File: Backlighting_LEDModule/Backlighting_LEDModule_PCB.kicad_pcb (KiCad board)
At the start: 2 copper layers, 32.2 x 55 mm, 6 parts, among them J1 Conn_02x10_Odd_Even, J11 BOARD_CONN, J2 Conn_02x10_Odd_Even

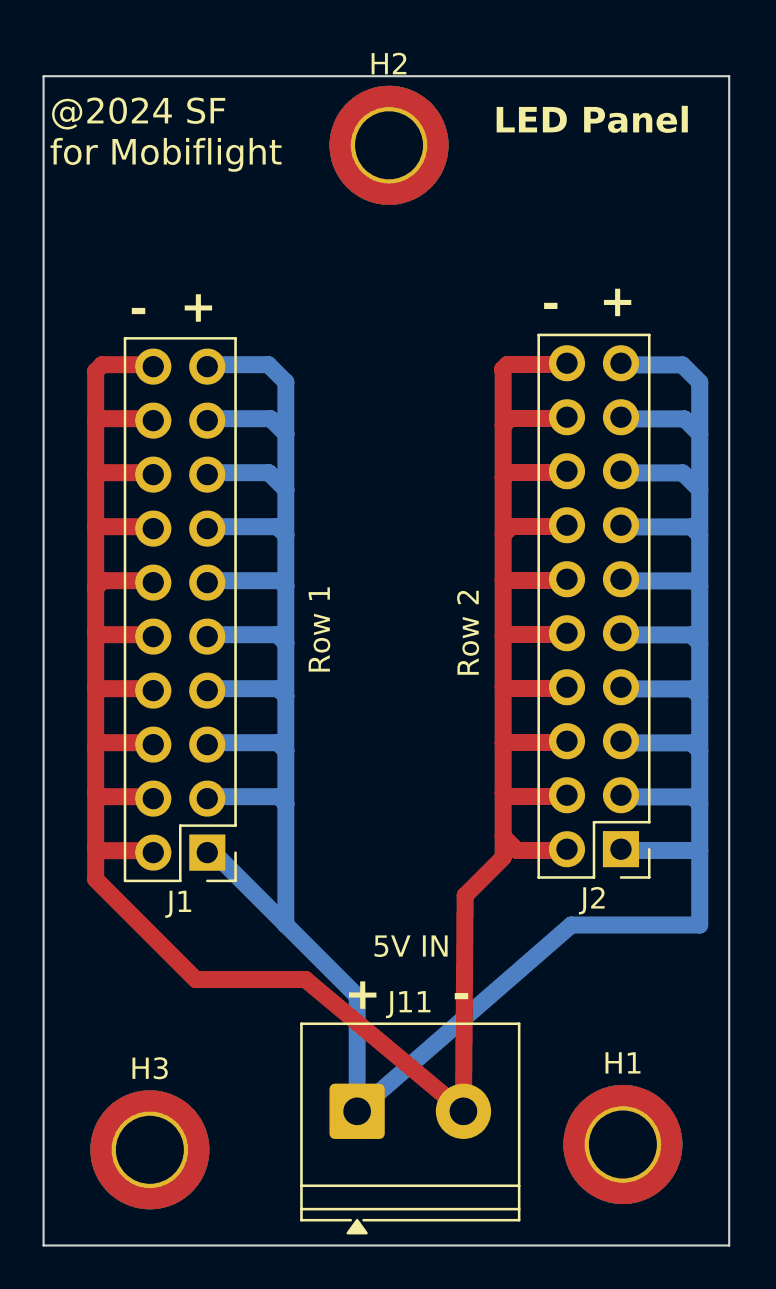
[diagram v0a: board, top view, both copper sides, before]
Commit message: Update the last three boards from the library
Aggiornati i footprint di LEDModule, Korry grande e Korry piccolo, come era
gia' stato fatto sul dimmer. Le quattordici lib_footprint_mismatch che
restavano sono chiuse.

Le serigrafie hanno retto anche qui: 220, 91, BK_LED e BTN+LED sono ancora
su F.Silk su tutti e due i Korry, e tutte le scritte libere sono al loro
posto. Piste e posizioni dei componenti invariate: 128, 28 e 28 tratti,
stessi estremi e stesse larghezze.

L'aggiornamento ha allargato di poco il contorno di J2 sul Korry piccolo, e
la scritta '+5' arrivava a 0.09 mm da esso. A sinistra non poteva andare,
perche' partiva gia' 0.15 mm fuori dal bordo scheda: e' diventata '+', e per
coerenza la 'L' dell'altro piolo e' diventata '-'. Ora quel connettore e'
marcato come quello del Korry grande e come le file del LEDModule.

Nota per la prossima volta: il font a tratti di KiCad avanza circa 1.0 em
per carattere, non 0.72 come stimava il mio controllo. Per questo un paio di
scritte che avevo dato per libere sono poi state prese dal DRC.

Co-Authored-By: Claude Opus 5 <noreply@anthropic.com>
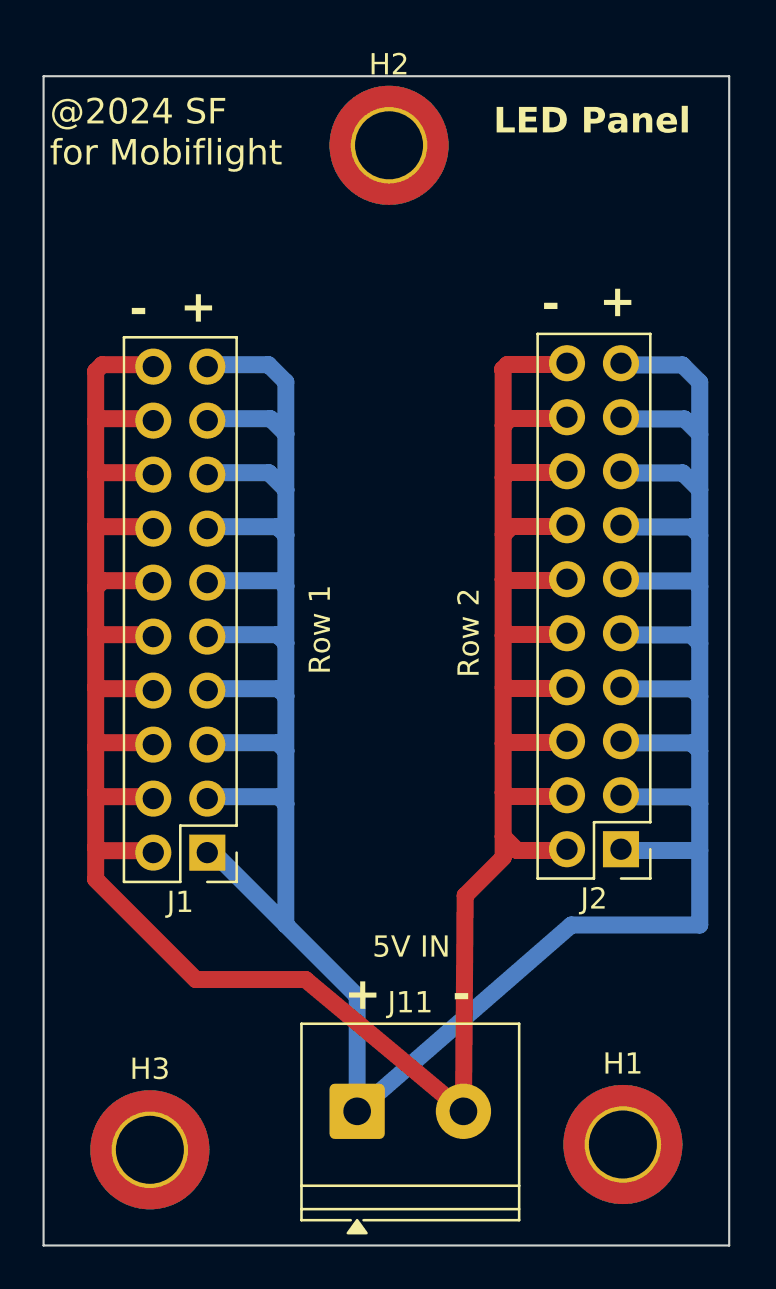
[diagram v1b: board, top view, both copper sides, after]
